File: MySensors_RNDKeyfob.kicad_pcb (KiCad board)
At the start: 2 copper layers, 27 x 42.9 mm, 21 parts, among them P1 CONN_01X01, P2 CONN_02X03, SW1 SW_SPST, SW2 SW_SPST, SW3 SW_SPST, SW4 SW_SPST, SW5 SW_SPST, U1 ATSHA204A, U2 RFM69HCW, U3 ATMEGA328P-MU

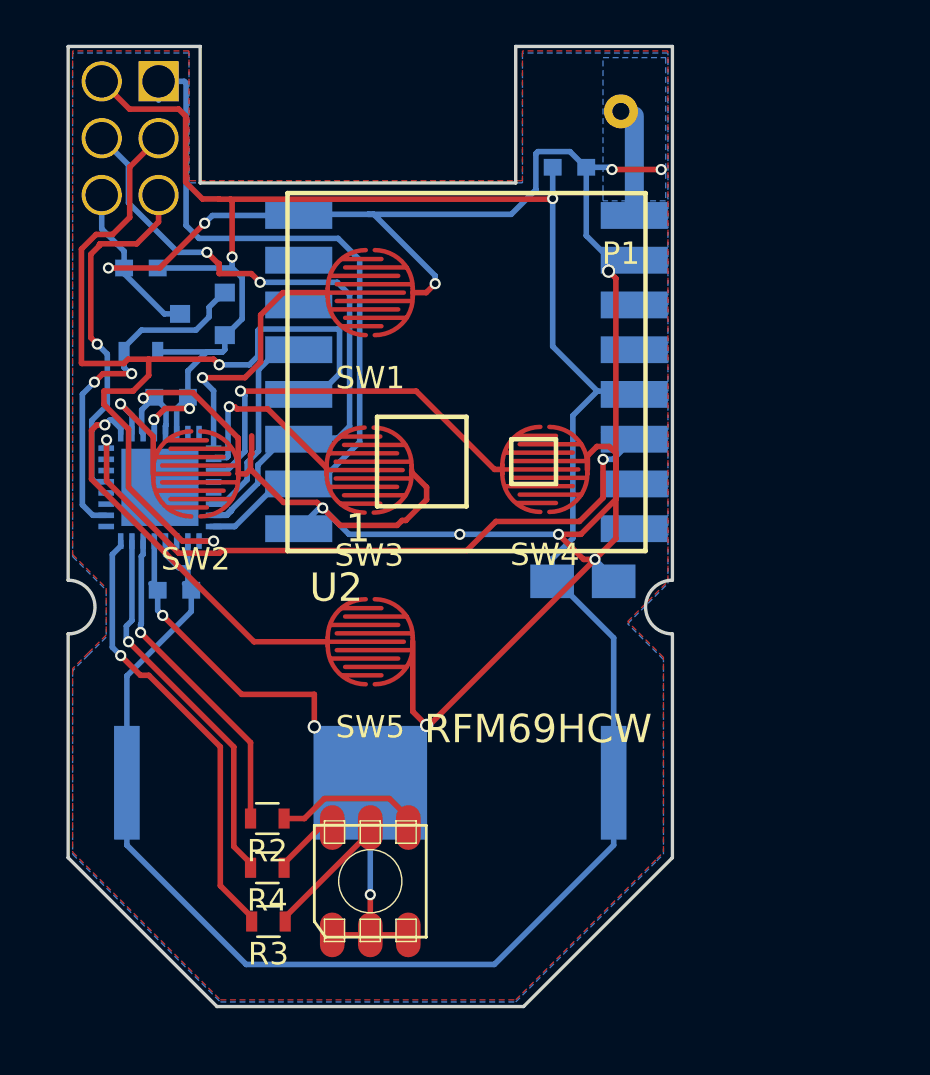
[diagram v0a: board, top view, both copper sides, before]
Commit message: Doubled size of battery pads. Added HT7333 to allow for LIR2032 lithium coin cell (Bridge pads for CR2032). Changed A7 to A2 to make LED work. Added SMD contacts for TX and GND for debug output (interface with pogo pins).
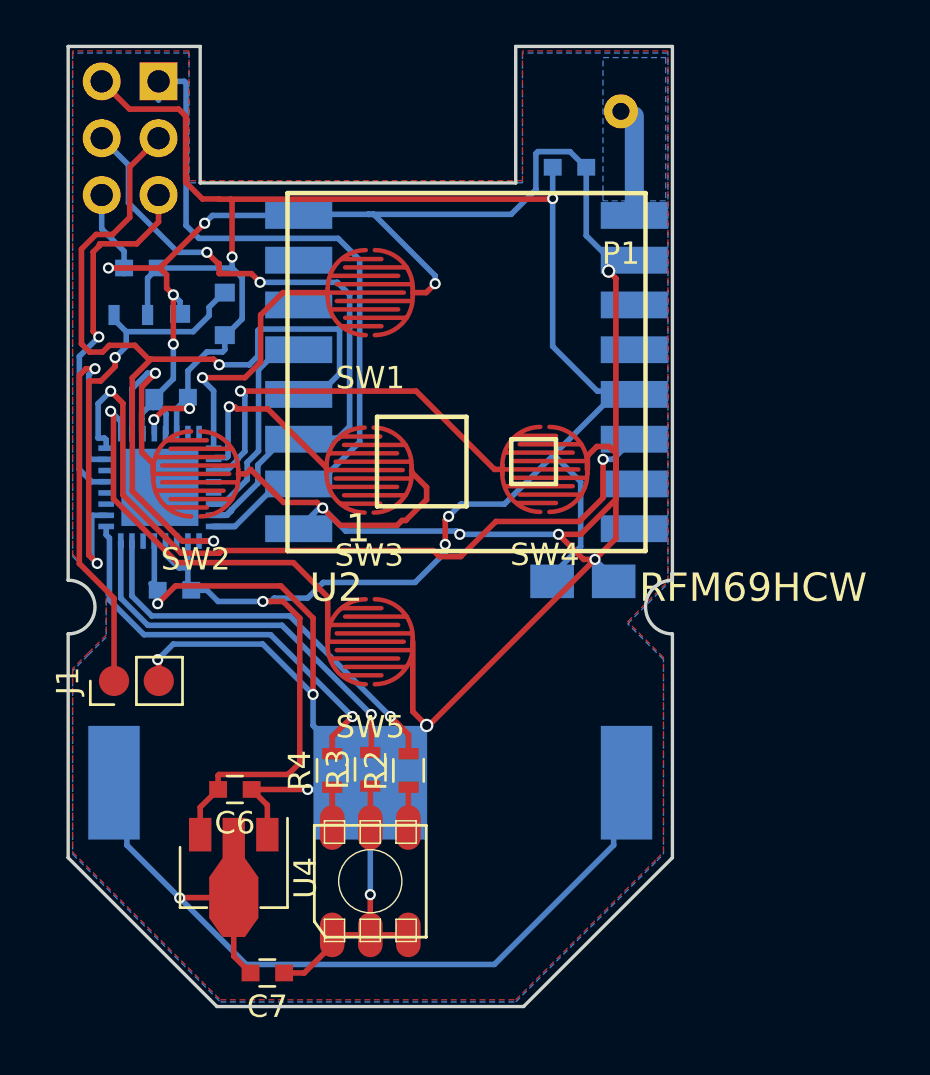
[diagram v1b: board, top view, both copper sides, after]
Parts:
- added C6: C, Capacitors_SMD:C_0603, F.Cu at (193.9, 90.3)
- added C7: C, Capacitors_SMD:C_0603, F.Cu at (195.4, 98.5)
- added J1: CONN_01X02, Pin_Headers:Pin_Header_Straight_1x02_Pitch2.00mm, F.Cu at (188.6, 85.5)
- added U4: HT7333, TO_SOT_Packages_SMD:SOT-89-3, F.Cu at (193.9, 93.8)
- moved R3 8.18 mm to (200.0, 89.4), turned to 90 degrees
- moved R2 6.67 mm to (201.7, 89.5), turned to 90 degrees
- moved R4 5.23 mm to (198.3, 89.5), turned to 90 degrees
- moved R1 1.71 mm to (189.3, 69.1)
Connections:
- BT1 pad 1: /VCC -> Net-(BT1-Pad1)
- R2 pad 2: /A7 -> /A0
- R4 pad 2: /A0 -> /A2
- U3 pad 22: /A7 -> (no net)
- U3 pad 25: (no net) -> /A2
- U3 pad 31: (no net) -> /TXO
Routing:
- net Net-(BT1-Pad1): track 0.00 -> 40.5 mm, vias 0 -> 1
- net /TXO: track 0.00 -> 20.0 mm, vias 0 -> 1
- net /A2: track 0.00 -> 18.4 mm, vias 0 -> 1
- net GND: track 157.4 -> 175.1 mm, vias 15 -> 16
- net /VCC: track 125.5 -> 110.8 mm, vias 4 -> 7
- net /A7: track 14.5 -> 0.00 mm, vias 1 -> 0
- net /D2: track 31.6 -> 36.4 mm
- net /A3: track 15.9 -> 20.7 mm
- net Net-(D1-Pad4): track 6.72 -> 2.26 mm
- net Net-(D1-Pad5): track 5.77 -> 2.05 mm
- net /D4: track 5.27 -> 8.31 mm
- net /SCK: track 43.6 -> 41.4 mm
- net /A1: track 20.0 -> 17.8 mm
- net /A0: track 17.0 -> 18.2 mm
- net Net-(D1-Pad6): track 3.01 -> 1.80 mm
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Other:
- net class Default: clearance 0.17 -> 0.16
- rule trace_clearance: 0.17 -> 0.16
